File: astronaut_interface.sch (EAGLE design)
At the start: 17 parts, among them IC1 PCF8591T, J1 User Interface (I2C), J2 Display (I2C), P1 JT9S-19

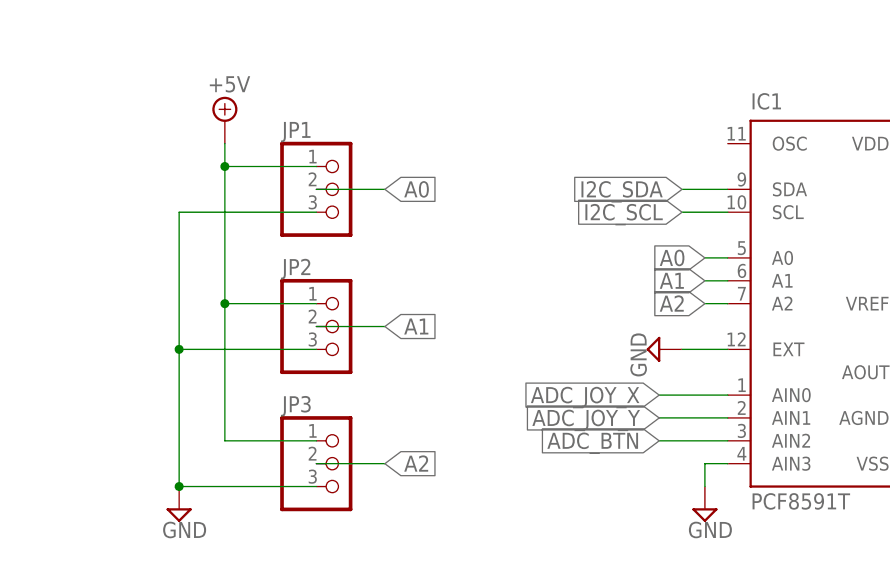
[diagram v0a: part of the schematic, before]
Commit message: added boards for astronaut
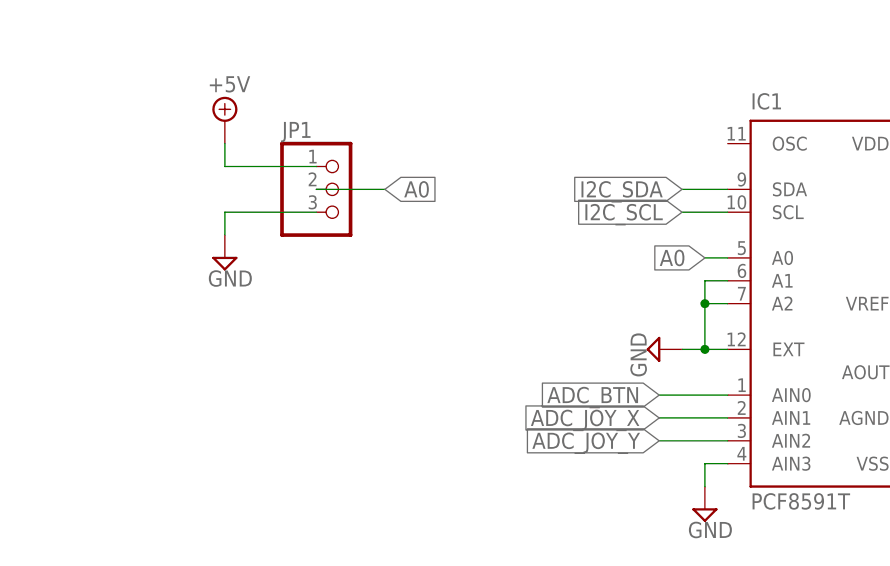
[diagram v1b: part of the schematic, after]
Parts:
- removed JP2, JP3: (no value), pinhead:PINHD-1X3
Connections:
- removed net A1: IC1.A1, JP2.2
- removed net A2: IC1.A2, JP3.2
- net +5V: no longer JP2.1, JP3.1
- net ADC_BTN: now also IC1.AIN0; no longer IC1.AIN2
- net ADC_JOY_X: now also IC1.AIN1; no longer IC1.AIN0
- net ADC_JOY_Y: now also IC1.AIN2; no longer IC1.AIN1
- net GND: now also IC1.A1, IC1.A2; no longer JP2.3, JP3.3
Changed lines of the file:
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@@
 <part name="SUPPLY12" library="supply2" deviceset="GND" device=""/>
 <part name="JP1" library="pinhead" deviceset="PINHD-1X3" device=""/>
-<part name="JP2" library="pinhead" deviceset="PINHD-1X3" device=""/>
-<part name="JP3" library="pinhead" deviceset="PINHD-1X3" device=""/>
 <part name="R5" library="resistor" deviceset="R-EU_" device="M0805" value="470"/>
 <part name="R6" library="resistor" deviceset="R-EU_" device="M0805" value="470"/>
@@
 <instance part="SUPPLY12" gate="GND" x="175.26" y="-43.18"/>
 <instance part="JP1" gate="A" x="134.62" y="-7.62"/>
-<instance part="JP2" gate="A" x="134.62" y="-22.86"/>
-<instance part="JP3" gate="A" x="134.62" y="-38.1"/>
 <instance part="R5" gate="G$1" x="182.88" y="50.8" rot="R90"/>
 <instance part="R6" gate="G$1" x="175.26" y="50.8" rot="R90"/>
 <instance part="SUPPLY13" gate="+5V" x="121.92" y="0"/>
-<instance part="SUPPLY14" gate="GND" x="116.84" y="-43.18"/>
+<instance part="SUPPLY14" gate="GND" x="121.92" y="-15.24"/>
 </instances>
 <busses>
@@
 <pinref part="SUPPLY10" gate="GND" pin="GND"/>
 <pinref part="IC1" gate="G$1" pin="EXT"/>
-<wire x1="172.72" y1="-25.4" x2="177.8" y2="-25.4" width="0.1524" layer="91"/>
+<wire x1="172.72" y1="-25.4" x2="175.26" y2="-25.4" width="0.1524" layer="91"/>
+<pinref part="IC1" gate="G$1" pin="A2"/>
+<wire x1="175.26" y1="-25.4" x2="177.8" y2="-25.4" width="0.1524" layer="91"/>
+<wire x1="177.8" y1="-20.32" x2="175.26" y2="-20.32" width="0.1524" layer="91"/>
+<wire x1="175.26" y1="-20.32" x2="175.26" y2="-25.4" width="0.1524" layer="91"/>
+<junction x="175.26" y="-25.4"/>
+<pinref part="IC1" gate="G$1" pin="A1"/>
+<wire x1="177.8" y1="-17.78" x2="175.26" y2="-17.78" width="0.1524" layer="91"/>
+<wire x1="175.26" y1="-17.78" x2="175.26" y2="-20.32" width="0.1524" layer="91"/>
+<junction x="175.26" y="-20.32"/>
 </segment>
 <segment>
@@
 <pinref part="JP1" gate="A" pin="3"/>
 <pinref part="SUPPLY14" gate="GND" pin="GND"/>
-<wire x1="132.08" y1="-10.16" x2="116.84" y2="-10.16" width="0.1524" layer="91"/>
-<wire x1="116.84" y1="-10.16" x2="116.84" y2="-25.4" width="0.1524" layer="91"/>
-<pinref part="JP2" gate="A" pin="3"/>
-<wire x1="116.84" y1="-25.4" x2="116.84" y2="-40.64" width="0.1524" layer="91"/>
-<wire x1="132.08" y1="-25.4" x2="116.84" y2="-25.4" width="0.1524" layer="91"/>
-<junction x="116.84" y="-25.4"/>
-<pinref part="JP3" gate="A" pin="3"/>
-<wire x1="132.08" y1="-40.64" x2="116.84" y2="-40.64" width="0.1524" layer="91"/>
-<junction x="116.84" y="-40.64"/>
+<wire x1="132.08" y1="-10.16" x2="121.92" y2="-10.16" width="0.1524" layer="91"/>
+<wire x1="121.92" y1="-10.16" x2="121.92" y2="-12.7" width="0.1524" layer="91"/>
 </segment>
 </net>
@@
 <wire x1="132.08" y1="-5.08" x2="121.92" y2="-5.08" width="0.1524" layer="91"/>
 <wire x1="121.92" y1="-5.08" x2="121.92" y2="-2.54" width="0.1524" layer="91"/>
-<pinref part="JP2" gate="A" pin="1"/>
-<wire x1="132.08" y1="-20.32" x2="121.92" y2="-20.32" width="0.1524" layer="91"/>
-<wire x1="121.92" y1="-20.32" x2="121.92" y2="-5.08" width="0.1524" layer="91"/>
-<junction x="121.92" y="-5.08"/>
-<pinref part="JP3" gate="A" pin="1"/>
-<wire x1="132.08" y1="-35.56" x2="121.92" y2="-35.56" width="0.1524" layer="91"/>
-<wire x1="121.92" y1="-35.56" x2="121.92" y2="-20.32" width="0.1524" layer="91"/>
-<junction x="121.92" y="-20.32"/>
 </segment>
 </net>
@@
 </segment>
 <segment>
-<pinref part="IC1" gate="G$1" pin="AIN2"/>
-<wire x1="177.8" y1="-35.56" x2="170.18" y2="-35.56" width="0.1524" layer="91"/>
-<label x="170.18" y="-35.56" size="1.778" layer="95" rot="R180" xref="yes"/>
+<pinref part="IC1" gate="G$1" pin="AIN0"/>
+<wire x1="177.8" y1="-30.48" x2="170.18" y2="-30.48" width="0.1524" layer="91"/>
+<label x="170.18" y="-30.48" size="1.778" layer="95" rot="R180" xref="yes"/>
 </segment>
 </net>
@@
 </segment>
 <segment>
+<pinref part="IC1" gate="G$1" pin="AIN2"/>
+<wire x1="177.8" y1="-35.56" x2="170.18" y2="-35.56" width="0.1524" layer="91"/>
+<label x="170.18" y="-35.56" size="1.778" layer="95" rot="R180" xref="yes"/>
+</segment>
+</net>
+<net name="ADC_JOY_X" class="0">
+<segment>
+<pinref part="P1" gate="G$1" pin="XS"/>
+<wire x1="63.5" y1="-33.02" x2="66.04" y2="-33.02" width="0.1524" layer="91"/>
+<label x="66.04" y="-33.02" size="1.778" layer="95" xref="yes"/>
+</segment>
+<segment>
 <pinref part="IC1" gate="G$1" pin="AIN1"/>
 <wire x1="177.8" y1="-33.02" x2="170.18" y2="-33.02" width="0.1524" layer="91"/>
@@
 </segment>
 </net>
-<net name="ADC_JOY_X" class="0">
-<segment>
-<pinref part="P1" gate="G$1" pin="XS"/>
-<wire x1="63.5" y1="-33.02" x2="66.04" y2="-33.02" width="0.1524" layer="91"/>
-<label x="66.04" y="-33.02" size="1.778" layer="95" xref="yes"/>
-</segment>
-<segment>
-<pinref part="IC1" gate="G$1" pin="AIN0"/>
-<wire x1="177.8" y1="-30.48" x2="170.18" y2="-30.48" width="0.1524" layer="91"/>
-<label x="170.18" y="-30.48" size="1.778" layer="95" rot="R180" xref="yes"/>
-</segment>
-</net>
 <net name="A0" class="0">
 <segment>
@@
 </segment>
 </net>
-<net name="A1" class="0">
-<segment>
-<pinref part="JP2" gate="A" pin="2"/>
-<wire x1="132.08" y1="-22.86" x2="139.7" y2="-22.86" width="0.1524" layer="91"/>
-<label x="139.7" y="-22.86" size="1.778" layer="95" xref="yes"/>
-</segment>
-<segment>
-<pinref part="IC1" gate="G$1" pin="A1"/>
-<wire x1="175.26" y1="-17.78" x2="177.8" y2="-17.78" width="0.1524" layer="91"/>
-<label x="175.26" y="-17.78" size="1.778" layer="95" rot="R180" xref="yes"/>
-</segment>
-</net>
-<net name="A2" class="0">
-<segment>
-<pinref part="JP3" gate="A" pin="2"/>
-<wire x1="132.08" y1="-38.1" x2="139.7" y2="-38.1" width="0.1524" layer="91"/>
-<label x="139.7" y="-38.1" size="1.778" layer="95" xref="yes"/>
-</segment>
-<segment>
-<pinref part="IC1" gate="G$1" pin="A2"/>
-<wire x1="175.26" y1="-20.32" x2="177.8" y2="-20.32" width="0.1524" layer="91"/>
-<label x="175.26" y="-20.32" size="1.778" layer="95" rot="R180" xref="yes"/>
-</segment>
-</net>
